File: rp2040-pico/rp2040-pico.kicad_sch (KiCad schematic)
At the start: 4 parts

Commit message: Fixed reuse + updated schematic template
Reuse compatability has been fixed by updating the dep5 file.
Also updated template for schematic and filled in schematic info
fields.
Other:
- company: (none) -> Sidings Media
- title: (none) -> RP2040/Pico Main Control Board
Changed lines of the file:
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@@
-(kicad_sch (version 20210126) (generator eeschema)
+(kicad_sch (version 20211123) (generator eeschema)
   (paper "A4")
-  (no_connect (at 16.51 172.72))
+  (title_block
+    (title "RP2040/Pico Main Control Board")
+    (rev "0.1")
+    (company "Sidings Media")
+    (comment 1 "Licence: CERN-OHL-P-2.0 or any later version")
+  )
+  (no_connect (at 16.51 195.58))
   (no_connect (at 16.51 180.34))
   (no_connect (at 16.51 187.96))
-  (no_connect (at 16.51 195.58))
+  (no_connect (at 16.51 172.72))
   (symbol (lib_id "EuroCard160mmX100mm_holes:Mounting_Hole_PAD-Mechanical") (at 16.51 170.18 0) (unit 1)
     (in_bom yes) (on_board yes)

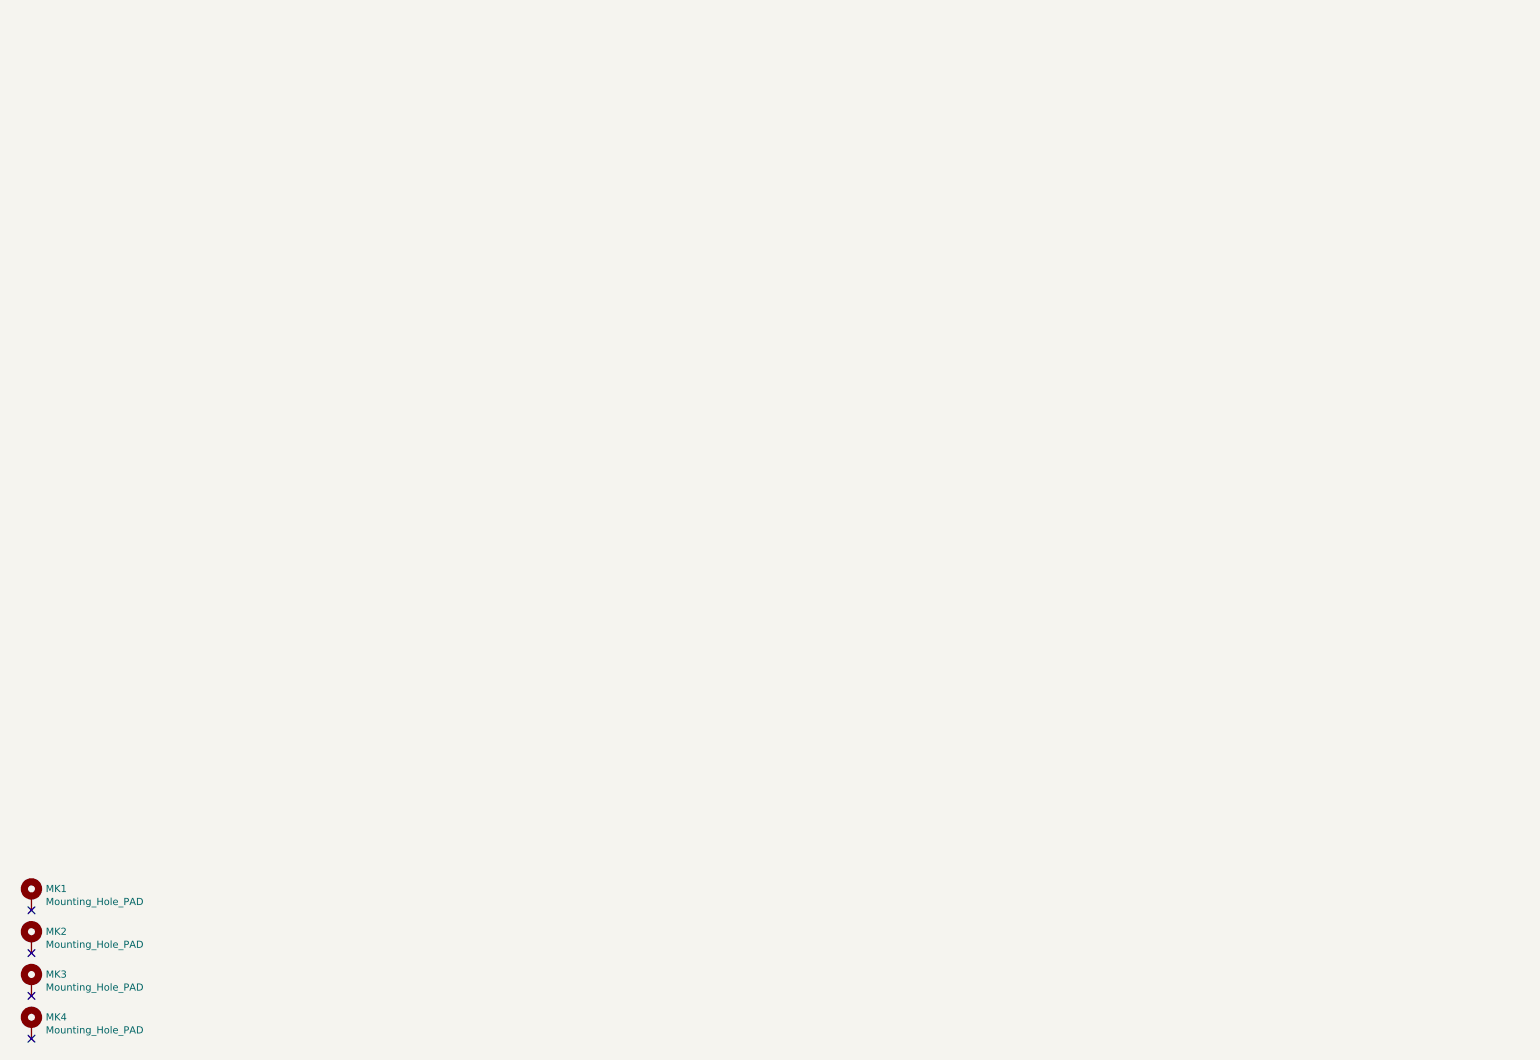
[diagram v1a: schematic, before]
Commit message: Initial board design
The initial design for the Rasbperry Pi Pico based board.
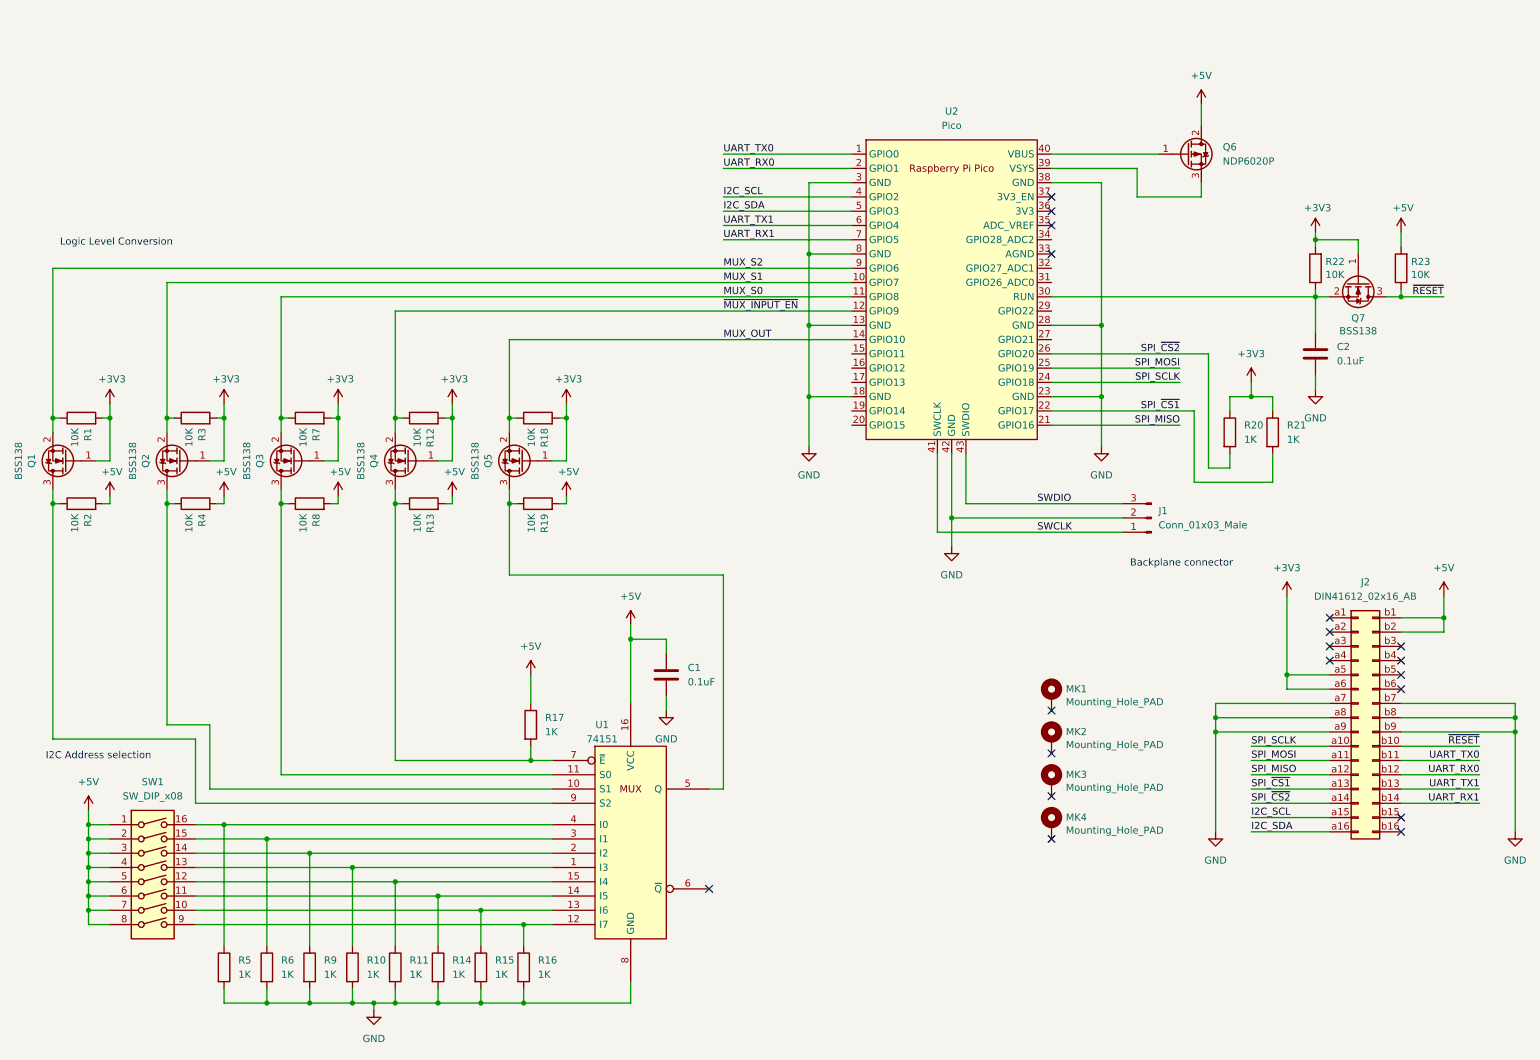
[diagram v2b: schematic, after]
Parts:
- added C1, C2: 0.1uF, Capacitor_THT:C_Disc_D4.7mm_W2.5mm_P5.00mm, symbol Device:C
- added J1: Conn_01x03_Male, symbol Connector:Conn_01x03_Male
- added J2: DIN41612_02x16_AB, symbol Connector:DIN41612_02x16_AB
- added Q1, Q2, Q3, Q4, Q5, Q7: BSS138, Package_TO_SOT_SMD:SOT-23, symbol Transistor_FET:BSS138
- added Q6: NDP6020P, Package_TO_SOT_THT:TO-220-3_Vertical, symbol Transistor_FET:FQP27P06
- added R1, R12, R13, R18, R19, R2, R22, R23, R3, R4, R7, R8: 10K, Resistor_SMD:R_0805_2012Metric, symbol Device:R
- added R10, R11, R14, R15, R16, R17, R20, R21, R5, R6, R9: 1K, Resistor_THT:R_Axial_DIN0207_L6.3mm_D2.5mm_P7.62mm_Horizontal, symbol Device:R
- added SW1: SW_DIP_x08, Package_DIP:DIP-16_W7.62mm, symbol Switch:SW_DIP_x08
- added U1: 74151, Package_DIP:DIP-16_W7.62mm, symbol 74xx_IEEE:74151
- added U2: Pico, MCU_RaspberryPi_and_Boards:RPi_Pico_SMD_TH, symbol MCU_RaspberryPi_and_Boards:Pico
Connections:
- new net: Q2.3 (D), R4.1, U1.10 (S1)
- new net: R10.1, SW1.13, U1.1 (I3)
- new net: Q3.3 (D), R8.1, U1.11 (S0)
- new net: R16.1, SW1.9, U1.12 (I7)
- new net: R15.1, SW1.10, U1.13 (I6)
- new net: R14.1, SW1.11, U1.14 (I5)
- new net: R11.1, SW1.12, U1.15 (I4)
- new net: R9.1, SW1.14, U1.2 (I2)
- new net: R6.1, SW1.15, U1.3 (I1)
- new net: R5.1, SW1.16, U1.4 (I0)
- new net: Q5.3 (D), R19.1, U1.5 (Q)
- new net: Q4.3 (D), R13.1, R17.2, U1.7 (~{E})
- new net: Q1.3 (D), R2.1, U1.9 (S2)
- new net: C2.1, Q7.2 (S), R22.1, U2.30 (RUN)
- new net: Q6.1 (G), U2.40 (VBUS)
- new net: Q6.3 (S), U2.39 (VSYS)
- new net +3V3: J2.a5 (Pin_a5), J2.a6 (Pin_a6), Q1.1 (G), Q2.1 (G), Q3.1 (G), Q4.1 (G), Q5.1 (G), Q7.1 (G), R1.2, R12.2, R18.2, R20.1, R21.1, R22.2, R3.2, R7.2
- new net +5V: C1.1, J2.b1 (Pin_b1), J2.b2 (Pin_b2), Q6.2 (D), R13.2, R17.1, R19.2, R2.2, R23.2, R4.2, R8.2, SW1.1, SW1.2, SW1.3, SW1.4, SW1.5, SW1.6, SW1.7, SW1.8, U1.16 (VCC)
- new net GND: C1.2, C2.2, J1.2 (Pin_2), J2.a7 (Pin_a7), J2.a8 (Pin_a8), J2.a9 (Pin_a9), J2.b7 (Pin_b7), J2.b8 (Pin_b8), J2.b9 (Pin_b9), R10.2, R11.2, R14.2, R15.2, R16.2, R5.2, R6.2, R9.2, U1.8 (GND), U2.13 (GND), U2.18 (GND), U2.23 (GND), U2.28 (GND), U2.3 (GND), U2.38 (GND), U2.42 (GND), U2.8 (GND)
- new net I2C_SCL: J2.a15 (Pin_a15), U2.4 (GPIO2)
- new net I2C_SDA: J2.a16 (Pin_a16), U2.5 (GPIO3)
- new net MUX_OUT: Q5.2 (S), R18.1, U2.14 (GPIO10)
- new net MUX_S0: Q3.2 (S), R7.1, U2.11 (GPIO8)
- new net MUX_S1: Q2.2 (S), R3.1, U2.10 (GPIO7)
- new net MUX_S2: Q1.2 (S), R1.1, U2.9 (GPIO6)
- new net SPI_MISO: J2.a12 (Pin_a12), U2.21 (GPIO16)
- new net SPI_MOSI: J2.a11 (Pin_a11), U2.25 (GPIO19)
- new net SPI_SCLK: J2.a10 (Pin_a10), U2.24 (GPIO18)
- new net SPI_~{CS1}: J2.a13 (Pin_a13), R21.2, U2.22 (GPIO17)
- new net SPI_~{CS2}: J2.a14 (Pin_a14), R20.2, U2.26 (GPIO20)
- new net SWCLK: J1.1 (Pin_1), U2.41 (SWCLK)
- new net SWDIO: J1.3 (Pin_3), U2.43 (SWDIO)
- new net UART_RX0: J2.b12 (Pin_b12), U2.2 (GPIO1)
- new net UART_RX1: J2.b14 (Pin_b14), U2.7 (GPIO5)
- new net UART_TX0: J2.b11 (Pin_b11), U2.1 (GPIO0)
- new net UART_TX1: J2.b13 (Pin_b13), U2.6 (GPIO4)
- new net ~{MUX_INPUT_EN}: Q4.2 (S), R12.1, U2.12 (GPIO9)
- new net ~{RESET}: J2.b10 (Pin_b10), Q7.3 (D), R23.1
- no-connect marks 4 -> 19
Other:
- note added: "Backplane connector"
- note added: "I2C Address selection"
- note added: "Logic Level Conversion"
- moved on the sheet: MK1, MK2, MK3, MK4

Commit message: Updated RP2040 schematic to include RP2040 + Pico
The schematic has been updated to now include the option to either use a
raspberry pi pico module, or to use an RP2040.
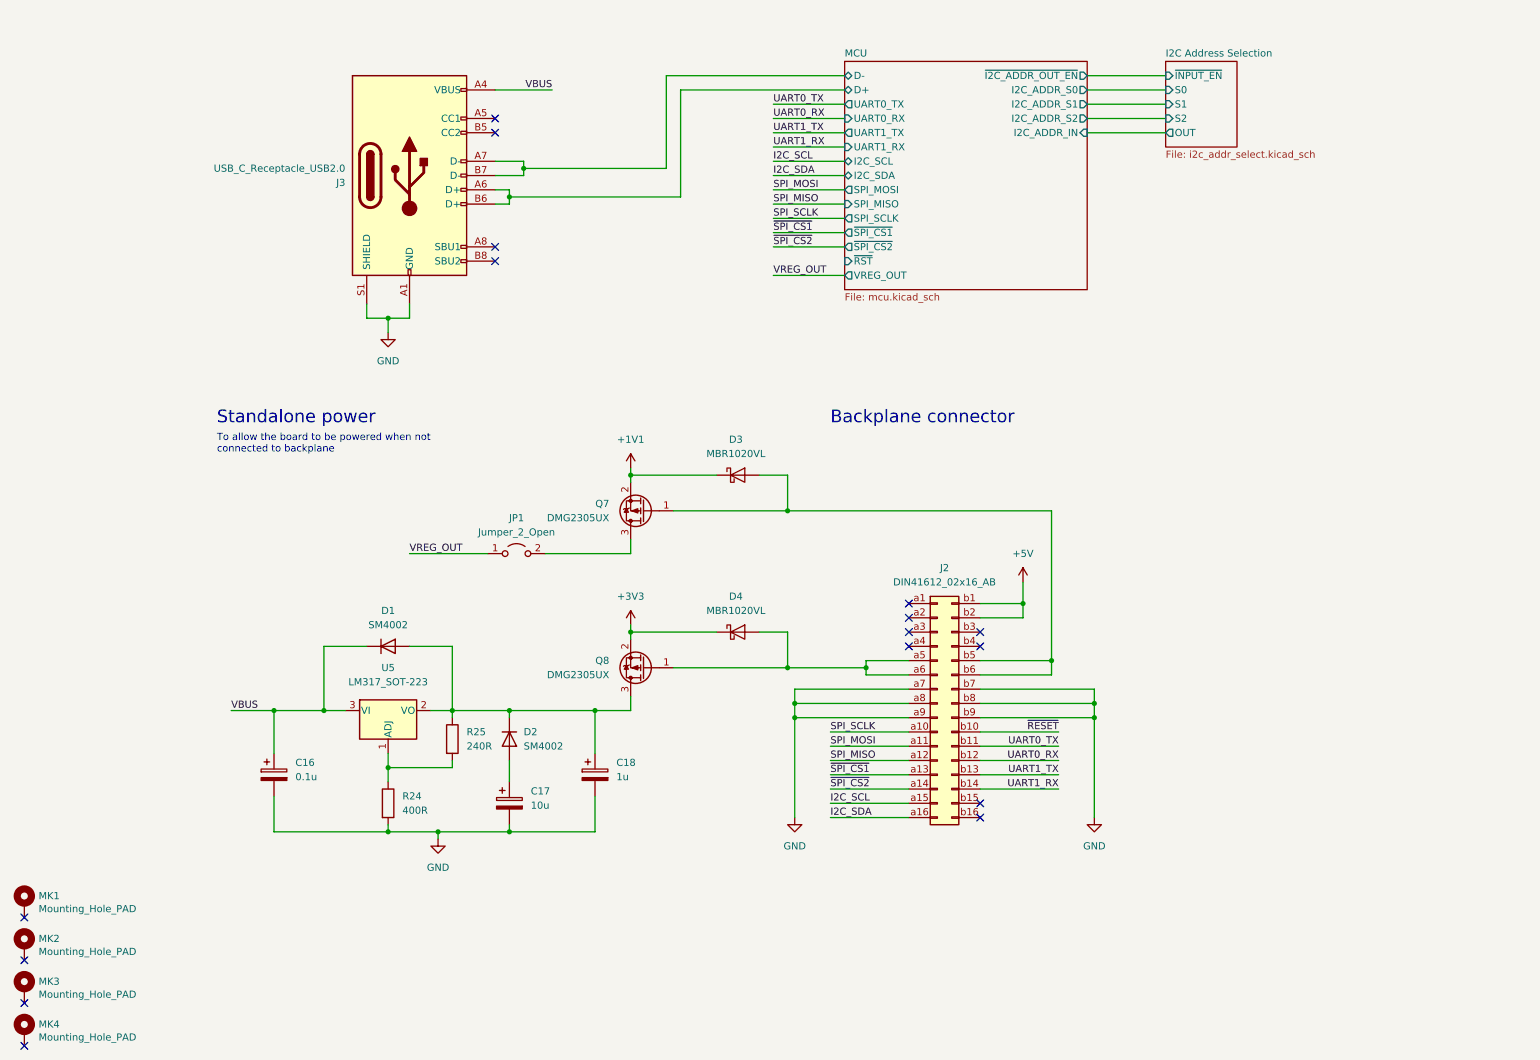
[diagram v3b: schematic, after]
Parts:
- removed C1, C2: 0.1uF, Capacitor_THT:C_Disc_D4.7mm_W2.5mm_P5.00mm, symbol Device:C
- removed J1: Conn_01x03_Male, symbol Connector:Conn_01x03_Male
- removed Q1, Q2, Q3, Q4, Q5, Q7: BSS138, Package_TO_SOT_SMD:SOT-23, symbol Transistor_FET:BSS138
- removed Q6: NDP6020P, Package_TO_SOT_THT:TO-220-3_Vertical, symbol Transistor_FET:FQP27P06
- removed R1, R12, R13, R18, R19, R2, R22, R23, R3, R4, R7, R8: 10K, Resistor_SMD:R_0805_2012Metric, symbol Device:R
- removed R10, R11, R14, R15, R16, R17, R20, R21, R5, R6, R9: 1K, Resistor_THT:R_Axial_DIN0207_L6.3mm_D2.5mm_P7.62mm_Horizontal, symbol Device:R
- removed SW1: SW_DIP_x08, Package_DIP:DIP-16_W7.62mm, symbol Switch:SW_DIP_x08
- removed U1: 74151, Package_DIP:DIP-16_W7.62mm, symbol 74xx_IEEE:74151
- removed U2: Pico, MCU_RaspberryPi_and_Boards:RPi_Pico_SMD_TH, symbol MCU_RaspberryPi_and_Boards:Pico
- added C16: 0.1u, symbol Device:C_Polarized
- added C17: 10u, symbol Device:C_Polarized
- added C18: 1u, symbol Device:C_Polarized
- added D1, D2: SM4002, Diode_SMD:D_MELF, symbol Diode:SM4002
- added D3, D4: MBR1020VL, Diode_SMD:D_SOD-123F, symbol Diode:MBR1020VL
- added J3: USB_C_Receptacle_USB2.0, symbol Connector:USB_C_Receptacle_USB2.0
- added JP1: Jumper_2_Open, symbol Jumper:Jumper_2_Open
- added Q7, Q8: DMG2305UX, Package_TO_SOT_SMD:SOT-23, symbol Transistor_FET:DMG2301L
- added R24: 400R, symbol Device:R
- added R25: 240R, symbol Device:R
- added U5: LM317_SOT-223, Package_TO_SOT_SMD:SOT-223-3_TabPin2, symbol Regulator_Linear:LM317_SOT-223
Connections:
- net +3V3: now also D4.1 (K), Q8.2 (S); no longer J2.a5 (Pin_a5), J2.a6 (Pin_a6)
- net GND: now also C16.2, C17.2, C18.2, J3.A1 (GND), J3.A12 (GND), J3.B1 (GND), J3.B12 (GND), J3.S1 (SHIELD), R24.2
- net at J2.b5 (Pin_b5): now also J2.b6 (Pin_b6), D3.2 (A), Q7.1 (G)
- net SPI_~{CS1} renamed ~{SPI_CS1}
- net SPI_~{CS2} renamed ~{SPI_CS2}
- net UART_RX0 renamed UART0_RX
- net UART_RX1 renamed UART1_RX
- net UART_TX0 renamed UART0_TX
- net UART_TX1 renamed UART1_TX
- new net: C17.1, D2.2 (A)
- new net: R24.1, R25.2, U5.1 (ADJ)
- new net: C18.1, D1.2 (A), D2.1 (K), Q8.3 (D), R25.1, U5.2 (VO)
- new net: D4.2 (A), J2.a5 (Pin_a5), J2.a6 (Pin_a6), Q8.1 (G)
- new net: JP1.2 (B), Q7.3 (D)
- new net +1V1: D3.1 (K), Q7.2 (S)
- new net MCU/D+: J3.A6 (D+), J3.B6 (D+)
- new net MCU/D-: J3.A7 (D-), J3.B7 (D-)
- new net VBUS: C16.1, D1.1 (K), J3.A4 (VBUS), J3.A9 (VBUS), J3.B4 (VBUS), J3.B9 (VBUS), U5.3 (VI)
- new net VREG_OUT: JP1.1 (A)
- no-connect marks 19 -> 16
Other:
- added sheet I2C Address Selection (i2c_addr_select.kicad_sch)
- added sheet MCU (mcu.kicad_sch)
- note added: "Standalone power"
- note added: "To allow the board to be powered when not connected to backplane"
- note removed: "I2C Address selection"
- note removed: "Logic Level Conversion"
- moved on the sheet: J2, MK1, MK2, MK3, MK4

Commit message: Added stat LEDs, BOOTSEL and reset button, SD card
3 LEDs have been added. One for indicating power and two for indicating
activity. Both activity LEDs are currently connected to the Pico/RP2040.
Buttons for boot selection and chip reset have been added to allow for
loading of firmware over USB. Support for a micro SD has also been
added. The card communicates with the Pico/RP2040 via the MCUs second
SPI interface and will store config files.

Signed-off-by: Matthew Nickson <mnickson@sidingsmedia.com>
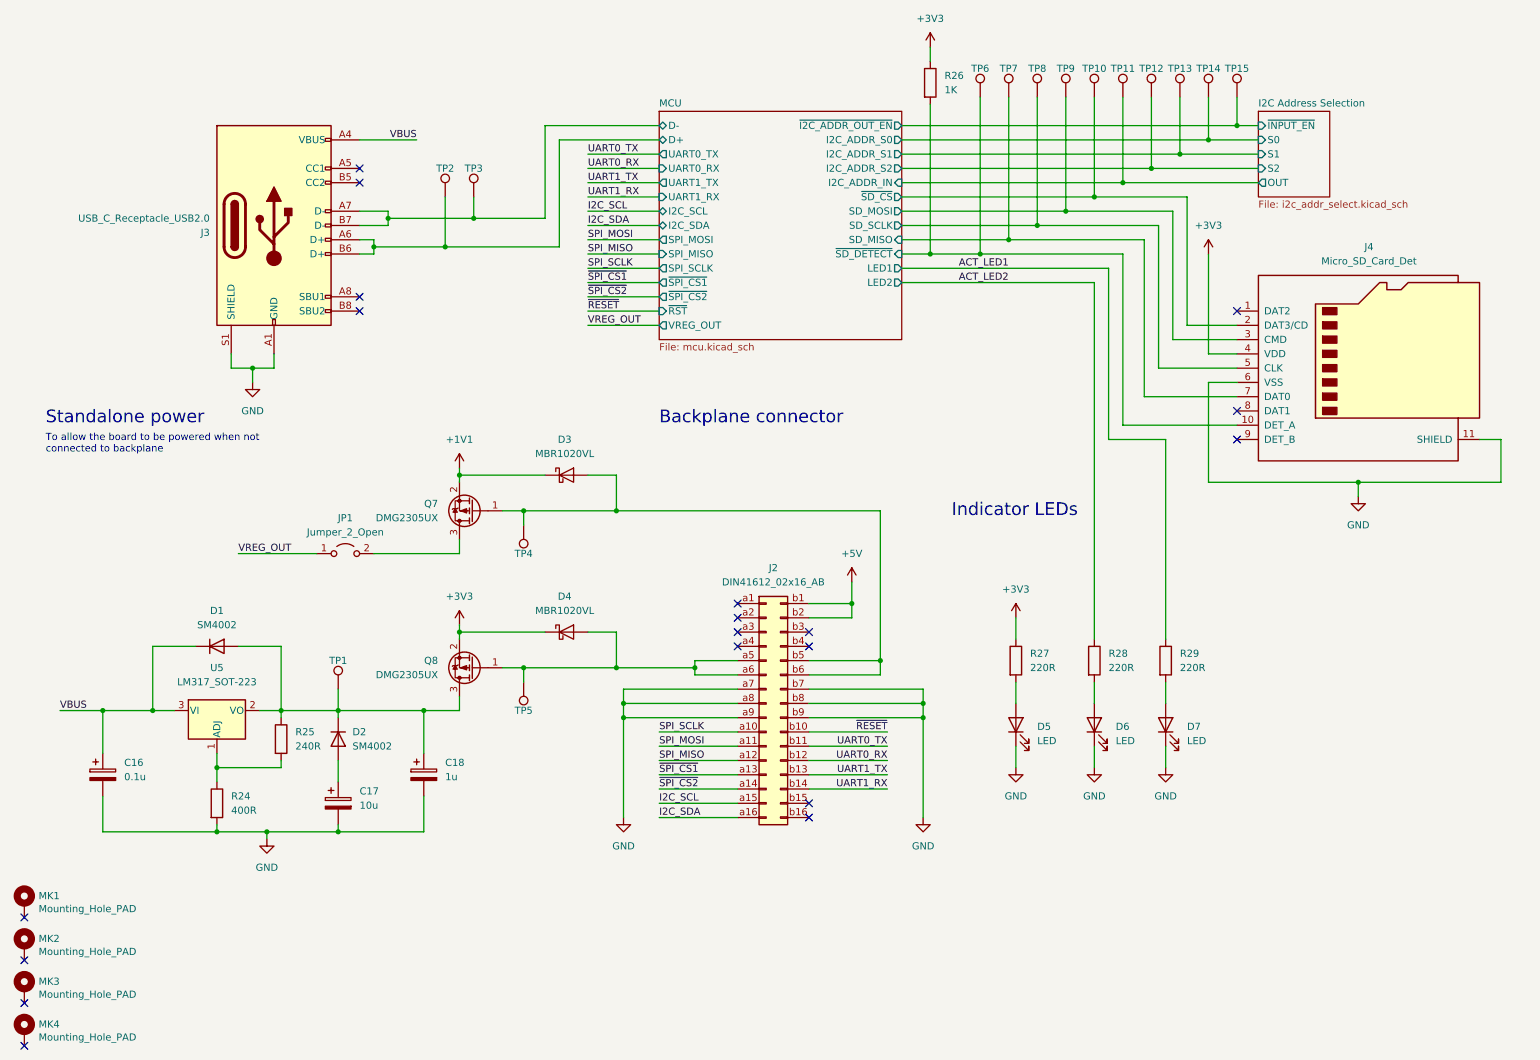
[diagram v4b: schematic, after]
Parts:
- added D5, D6, D7: LED, symbol Device:LED
- added J4: Micro_SD_Card_Det, symbol Connector:Micro_SD_Card_Det
- added R26: 1K, symbol Device:R
- added R27, R28, R29: 220R, symbol Device:R
- added TP1, TP10, TP11, TP12, TP13, TP14, TP15, TP2, TP3, TP4, TP5, TP6, TP7, TP8, TP9: TestPoint, symbol Connector:TestPoint
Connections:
- net +3V3: now also J4.4 (VDD), R26.1, R27.1
- net GND: now also D5.1 (K), D6.1 (K), D7.1 (K), J4.11 (SHIELD), J4.6 (VSS)
- net I2C Address Selection/OUT: now also TP11.1
- net I2C Address Selection/S0: now also TP14.1
- net I2C Address Selection/S1: now also TP13.1
- net I2C Address Selection/S2: now also TP12.1
- net I2C Address Selection/~{INPUT_EN}: now also TP15.1
- net MCU/D+: now also TP2.1
- net MCU/D-: now also TP3.1
- net at C18.1, D1.2 (A), D2.1 (K)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: now also TP1.1
- net at D4.2 (A), J2.a5 (Pin_a5), J2.a6 (Pin_a6)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: now also TP5.1
- net at D3.2 (A), J2.b5 (Pin_b5), J2.b6 (Pin_b6)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: now also TP4.1
- new net: D5.2 (A), R27.2
- new net: D6.2 (A), R28.2
- new net: D7.2 (A), R29.2
- new net ACT_LED1: R29.1
- new net ACT_LED2: R28.1
- new net MCU/SD_MISO: J4.7 (DAT0), TP7.1
- new net MCU/SD_MOSI: J4.3 (CMD), TP9.1
- new net MCU/SD_SCLK: J4.5 (CLK), TP8.1
- new net MCU/~{SD_CS}: J4.2 (DAT3/CD), TP10.1
- new net MCU/~{SD_DETECT}: J4.10 (DET_A), R26.2, TP6.1
- no-connect marks 16 -> 19
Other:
- sheet MCU ports: added LED1, LED2, SD_MISO, SD_MOSI, SD_SCLK, ~{SD_CS}, ~{SD_DETECT}; removed none
- note added: "Indicator LEDs"
- moved on the sheet: C16, C17, C18, D1, D2, D3, D4, J2, J3, JP1, Q7, Q8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
